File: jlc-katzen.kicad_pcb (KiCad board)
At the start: 4 copper layers, 59.4 x 52.2 mm, 62 parts, among them J1 USB_C_Receptacle_USB2.0_16P, J2 Conn_01x04, J3 Conn_01x04, J4 Conn_01x02, J5 Conn_ARM_SWD_TagConnect_TC2030, Q1 2N7002, Q2 2N7002, Q3 2N7002, U1 XC6206P332MR, U2 W25Q128JVSIQ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

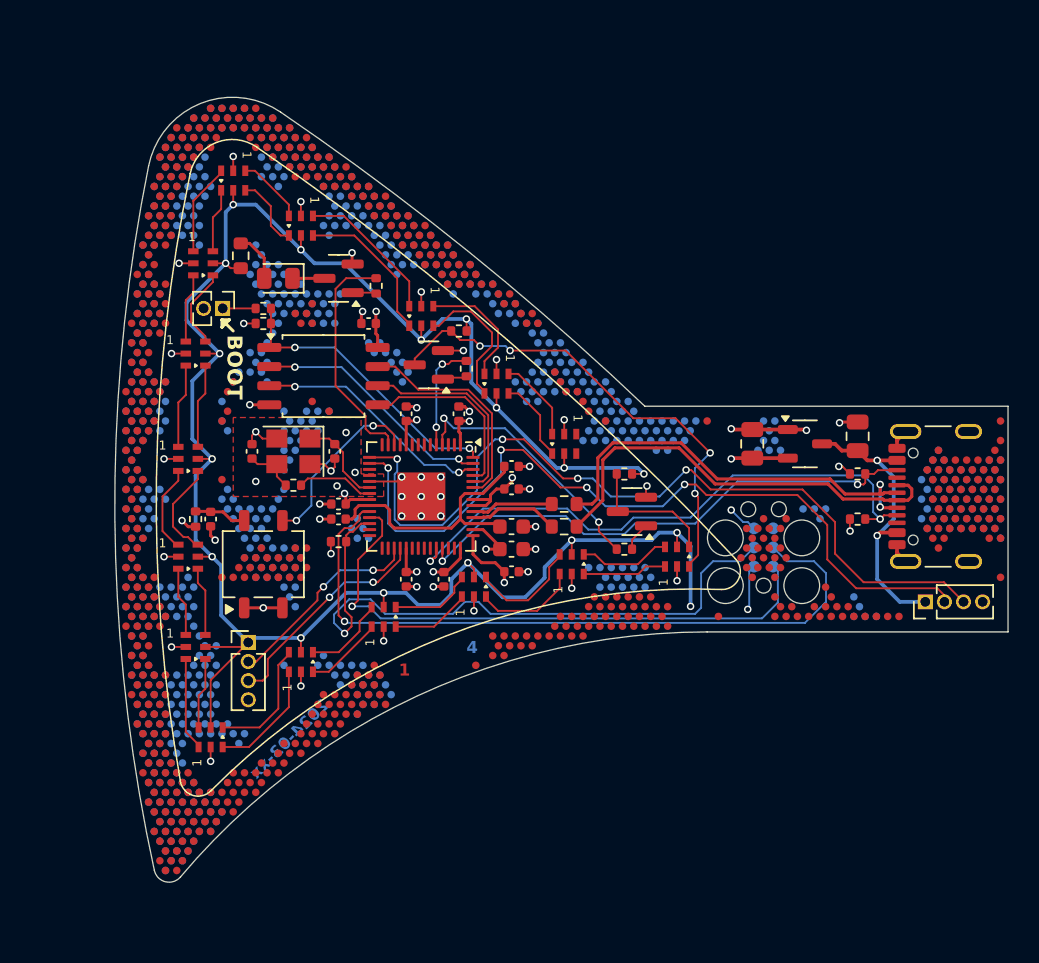
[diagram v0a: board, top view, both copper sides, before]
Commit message: thieving coverage not sufficient -> fill
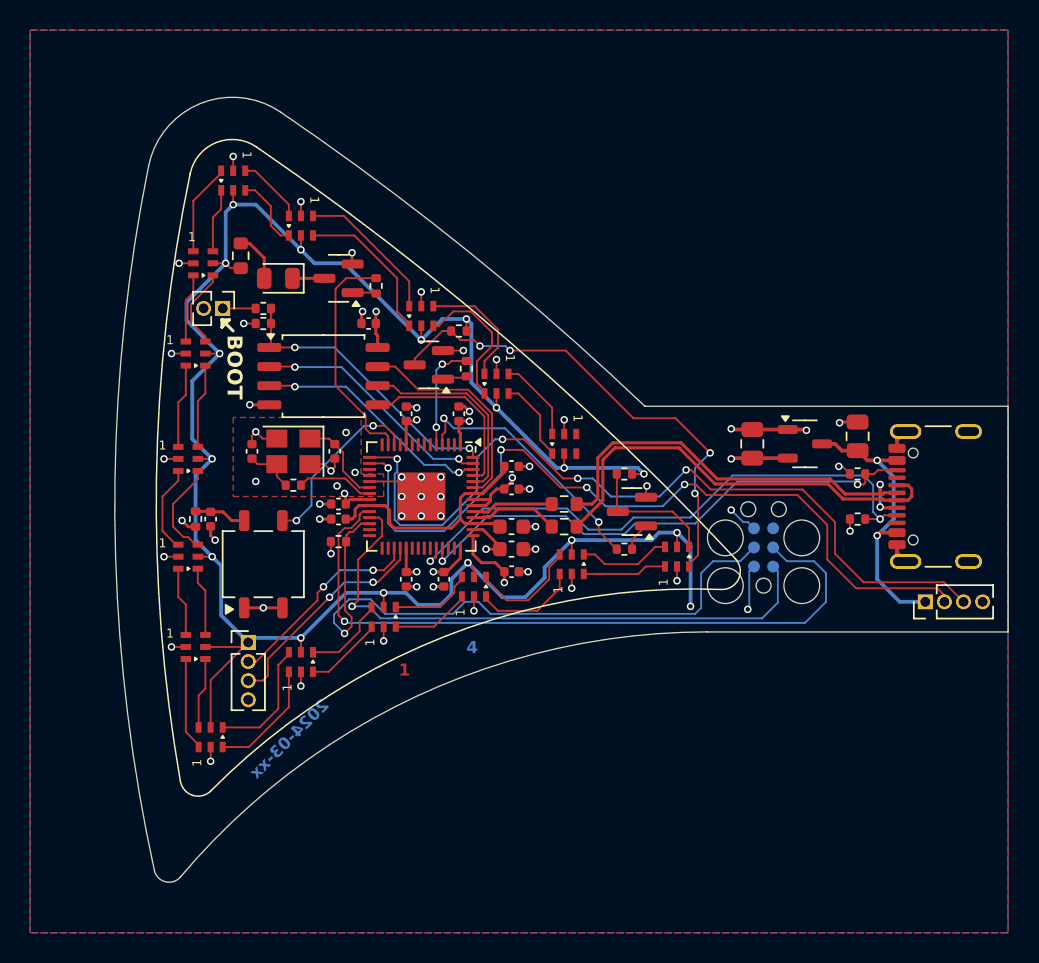
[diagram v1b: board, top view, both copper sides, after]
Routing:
- added copper zone on F.Cu, net (none)
- added copper zone on B.Cu, net GND
